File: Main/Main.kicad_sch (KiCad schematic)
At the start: 81 parts, among them J1 USB_B_Micro, J2 Micro_SD_Card, J3 Conn_01x03, J4 Conn_01x03, J5 Conn_01x03, J6 Conn_01x03, SW1 SW_Push, SW2 SW_Push, U1 RP2350A-QFN60, U10 LM75B, U11 MCS1802GS-50-Z, U12 MCS1802GS-50-Z, U13 MCS1802GS-50-Z, U14 LM2575-3.3BT, U2 W25Q128JVS, U3 AMS1117-3.3, U4 MMC5983MA, U5 ICM-42688-P, U6 INA226, U7 KX134-1211, U8 MS5611-01BA, U9 MCS1802GS-50-Z, Y1 ABM8-272-T3

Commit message: Added shunt footprint and small changes
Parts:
- removed R9: 2m, symbol Device:R_Shunt
- added R13: 2m, Resistor_SMD:R_1206_3216Metric, symbol Device:R
- C35, C36: footprint Capacitor_SMD:C_0805_2012Metric -> (none)
- D4: footprint Diode_SMD:D_0805_2012Metric -> (none)
- L2: footprint Inductor_SMD:L_0805_2012Metric -> (none)
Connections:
- net GND: now also U6.8 (Vbus), U6.9 (Vin-), R13.1
- net VSS: now also U6.10 (Vin+), R13.2
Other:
- note added: "High Precision 2mOhm Shunt"

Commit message: added button footprint
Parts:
- SW1, SW2: footprint (none) -> Button_Switch_SMD:SW_Push_SPST_NO_Alps_SKRK
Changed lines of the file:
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@@
 			)
 		)
-		(property "Footprint" ""
+		(property "Footprint" "Button_Switch_SMD:SW_Push_SPST_NO_Alps_SKRK"
 			(at 35.56 105.41 0)
 			(effects
@@
 			)
 		)
-		(property "Footprint" ""
+		(property "Footprint" "Button_Switch_SMD:SW_Push_SPST_NO_Alps_SKRK"
 			(at 139.7 115.57 0)
 			(effects

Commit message: updated usb footprint
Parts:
- J1: footprint (none) -> Connector_USB:USB_Micro-B_Amphenol_10118193-0001LF_Horizontal
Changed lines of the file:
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@@
 			)
 		)
-		(property "Footprint" ""
+		(property "Footprint" "Connector_USB:USB_Micro-B_Amphenol_10118193-0001LF_Horizontal"
 			(at 30.48 35.56 0)
 			(effects

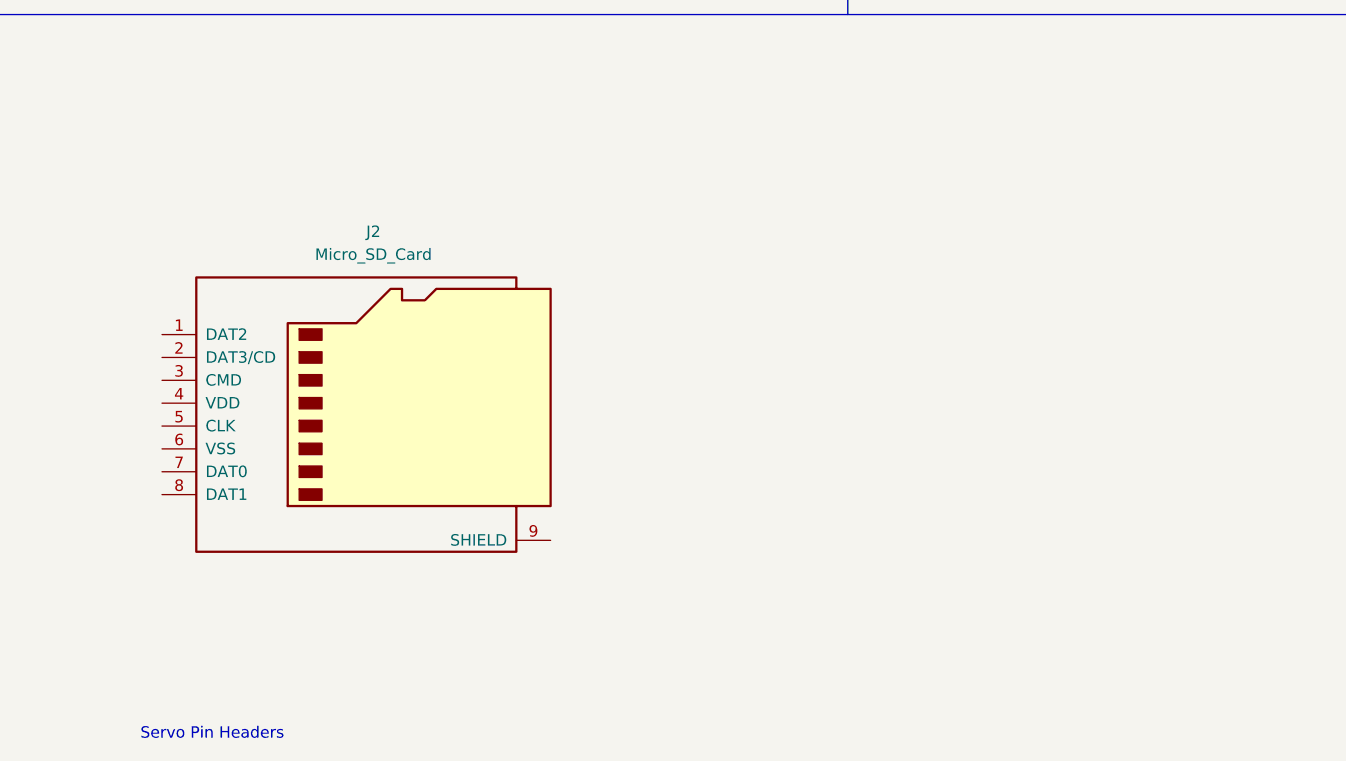
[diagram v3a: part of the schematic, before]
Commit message: SD and USB footprint and model updated
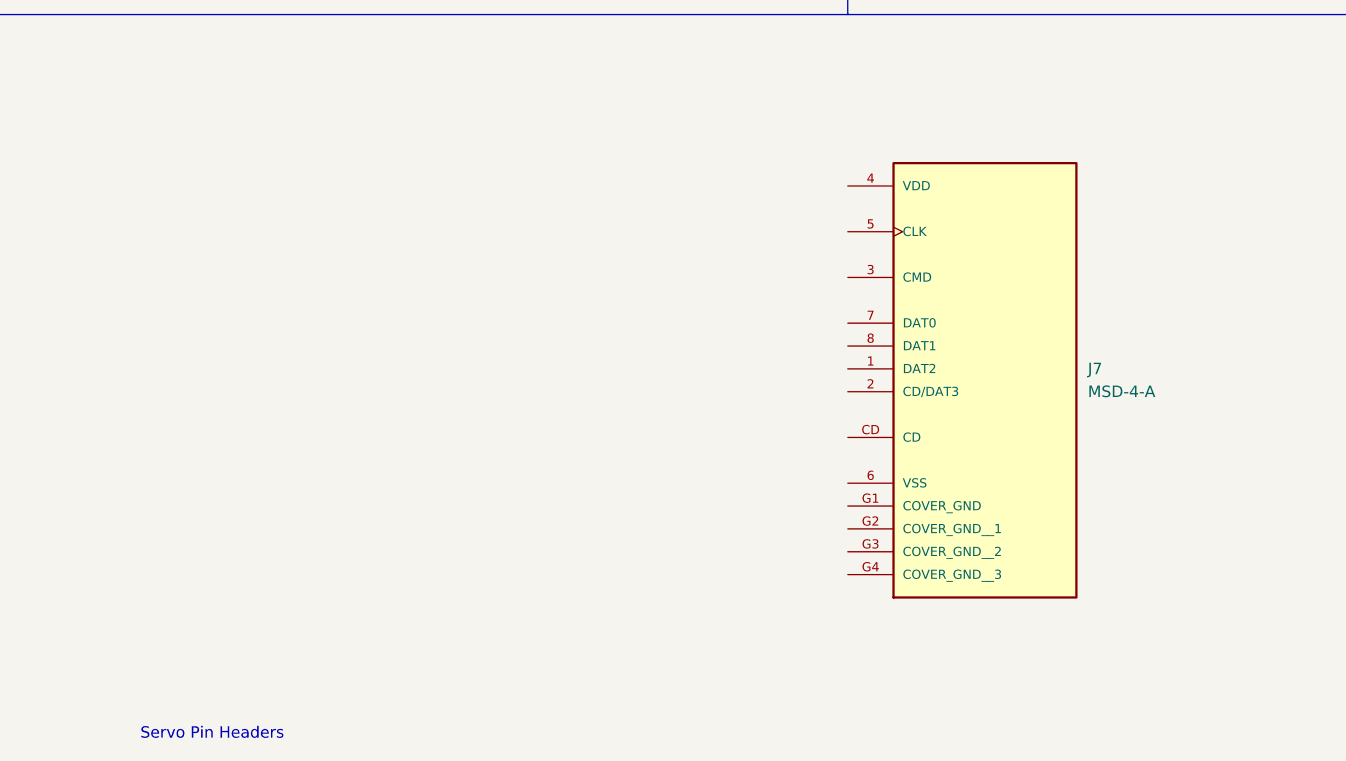
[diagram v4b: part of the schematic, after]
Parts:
- removed J2: Micro_SD_Card, symbol Connector:Micro_SD_Card
- added J7: MSD-4-A, otherComponents:CUI_MSD-4-A, symbol otherSymbols:MSD-4-A
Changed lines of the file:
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@@
 	)
 	(symbol
+		(lib_id "otherSymbols:MSD-4-A")
+		(at 391.16 267.97 0)
+		(unit 1)
+		(exclude_from_sim no)
+		(in_bom yes)
+		(on_board yes)
+		(dnp no)
+		(fields_autoplaced yes)
+		(property "Reference" "J7"
+			(at 402.59 270.5099 0)
+			(effects
+				(font
+					(size 1.27 1.27)
+				)
+				(justify left)
+			)
+		)
+		(property "Value" "MSD-4-A"
+			(at 402.59 273.0499 0)
+			(effects
+				(font
+					(size 1.27 1.27)
+				)
+				(justify left)
+			)
+		)
+		(property "Footprint" "otherComponents:CUI_MSD-4-A"
+			(at 391.16 267.97 0)
+			(effects
+				(font
+					(size 1.27 1.27)
+				)
+				(justify bottom)
+				(hide yes)
+			)
+		)
+		(property "Datasheet" ""
+			(at 391.16 267.97 0)
+			(effects
+				(font
+					(size 1.27 1.27)
+				)
+				(hide yes)
+			)
+		)
+		(property "Description" ""
+			(at 391.16 267.97 0)
+			(effects
+				(font
+					(size 1.27 1.27)
+				)
+				(hide yes)
+			)
+		)
+		(property "PARTREV" "1.0"
+			(at 391.16 267.97 0)
+			(effects
+				(font
+					(size 1.27 1.27)
+				)
+				(justify bottom)
+				(hide yes)
+			)
+		)
+		(property "STANDARD" "Manufacturer Recommendations"
+			(at 391.16 267.97 0)
+			(effects
+				(font
+					(size 1.27 1.27)
+				)
+				(justify bottom)
+				(hide yes)
+			)
+		)
+		(property "MAXIMUM_PACKAGE_HEIGHT" "2.00mm"
+			(at 391.16 267.97 0)
+			(effects
+				(font
+					(size 1.27 1.27)
+				)
+				(justify bottom)
+				(hide yes)
+			)
+		)
+		(property "MANUFACTURER" "CUI Devices"
+			(at 391.16 267.97 0)
+			(effects
+				(font
+					(size 1.27 1.27)
+				)
+				(justify bottom)
+				(hide yes)
+			)
+		)
+		(pin "3"
+		)
+		(pin "G1"
+		)
+		(pin "G4"
+		)
+		(pin "7"
+		)
+		(pin "8"
+		)
+		(pin "G3"
+		)
+		(pin "4"
+		)
+		(pin "1"
+		)
+		(pin "2"
+		)
+		(pin "CD"
+		)
+		(pin "G2"
+		)
+		(pin "5"
+		)
+		(pin "6"
+		)
+		(instances
+			(project ""
+				(path "/6b66026e-3aa1-4d5a-a331-be21386153c7"
+					(reference "J7")
+					(unit 1)
+				)
+			)
+		)
+	)
+	(symbol
 		(lib_id "power:GND")
 		(at 274.32 43.18 0)
@@
 					(unit 1)
 				)
-			)
-		)
-	)
-	(symbol
-		(lib_id "Connector:Micro_SD_Card")
-		(at 322.58 274.32 0)
-		(unit 1)
-		(exclude_from_sim no)
-		(in_bom yes)
-		(on_board yes)
-		(dnp no)
-		(fields_autoplaced yes)
-		(property "Reference" "J2"
-			(at 323.215 255.27 0)
-			(effects
-				(font
-					(size 1.27 1.27)
-				)
-			)
-		)
-		(property "Value" "Micro_SD_Card"
-			(at 323.215 257.81 0)
-			(effects
-				(font
-					(size 1.27 1.27)
-				)
-			)
-		)
-		(property "Footprint" ""
-			(at 351.79 266.7 0)
-			(effects
-				(font
-					(size 1.27 1.27)
-				)
-				(hide yes)
-			)
-		)
-		(property "Datasheet" "https://www.we-online.com/components/products/datasheet/693072010801.pdf"
-			(at 322.58 274.32 0)
-			(effects
-				(font
-					(size 1.27 1.27)
-				)
-				(hide yes)
-			)
-		)
-		(property "Description" "Micro SD Card Socket"
-			(at 322.58 274.32 0)
-			(effects
-				(font
-					(size 1.27 1.27)
-				)
-				(hide yes)
-			)
-		)
-		(pin "9"
-		)
-		(pin "2"
-		)
-		(pin "3"
-		)
-		(pin "4"
-		)
-		(pin "5"
-		)
-		(pin "1"
-		)
-		(pin "6"
-		)
-		(pin "8"
-		)
-		(pin "7"
-		)
-		(instances
-			(project ""
-				(path "/6b66026e-3aa1-4d5a-a331-be21386153c7"
-					(reference "J2")
-					(unit 1)
-				)

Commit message: added xt60 connector
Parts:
- added J2: Conn_01x02, Connector_AMASS:AMASS_XT60-M_1x02_P7.20mm_Vertical, symbol Connector_Generic:Conn_01x02
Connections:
- net GND: now also J2.1 (Pin_1)
- net VIN: now also U11.1 (IP+), U11.2 (IP+), U12.1 (IP+), U12.2 (IP+), U13.1 (IP+), U13.2 (IP+), U9.1 (IP+), U9.2 (IP+), J2.2 (Pin_2)
- net current +: no longer U11.1 (IP+), U11.2 (IP+), U13.1 (IP+), U13.2 (IP+)
- net current -2: no longer U9.1 (IP+), U9.2 (IP+)
- net current -3: no longer U12.1 (IP+), U12.2 (IP+)
- net VOUT: no longer names the net of C36.1, L2.2, U14.4 (FB)
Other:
- note added: "figure out connection of 3.3v sources"

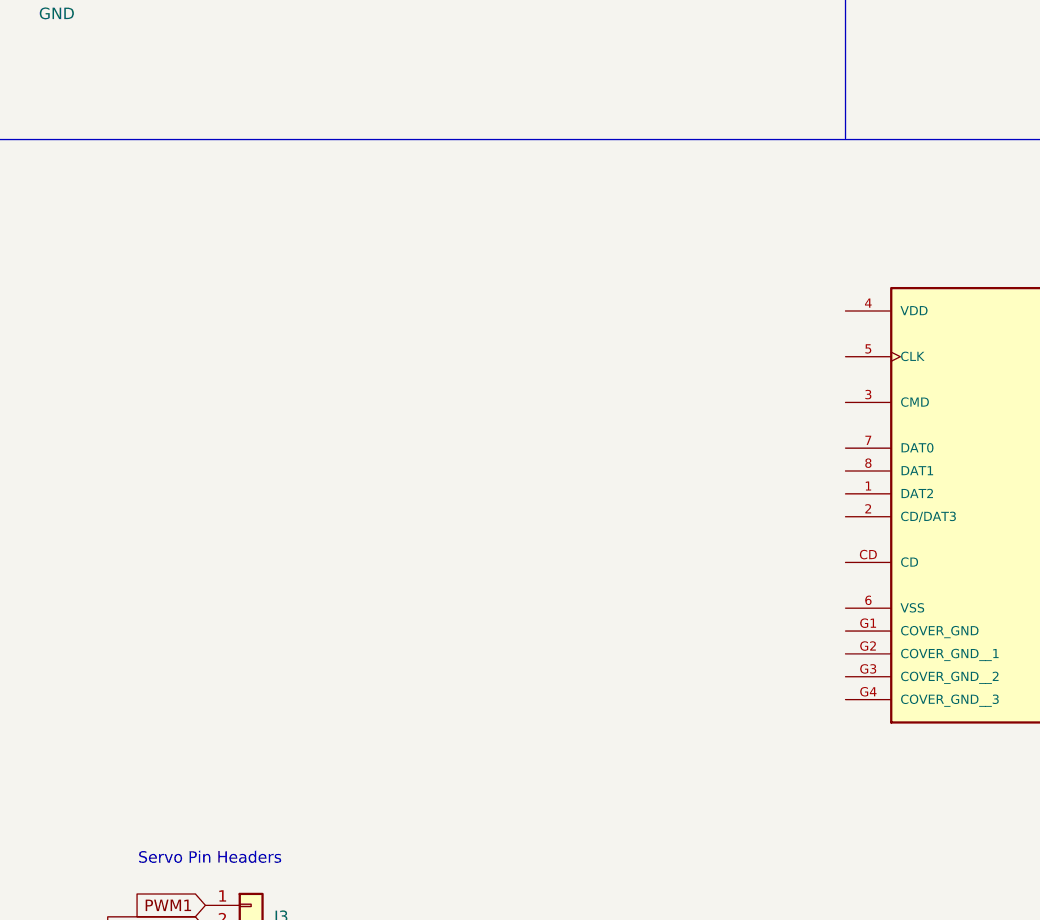
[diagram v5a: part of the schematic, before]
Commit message: added schematic sd card
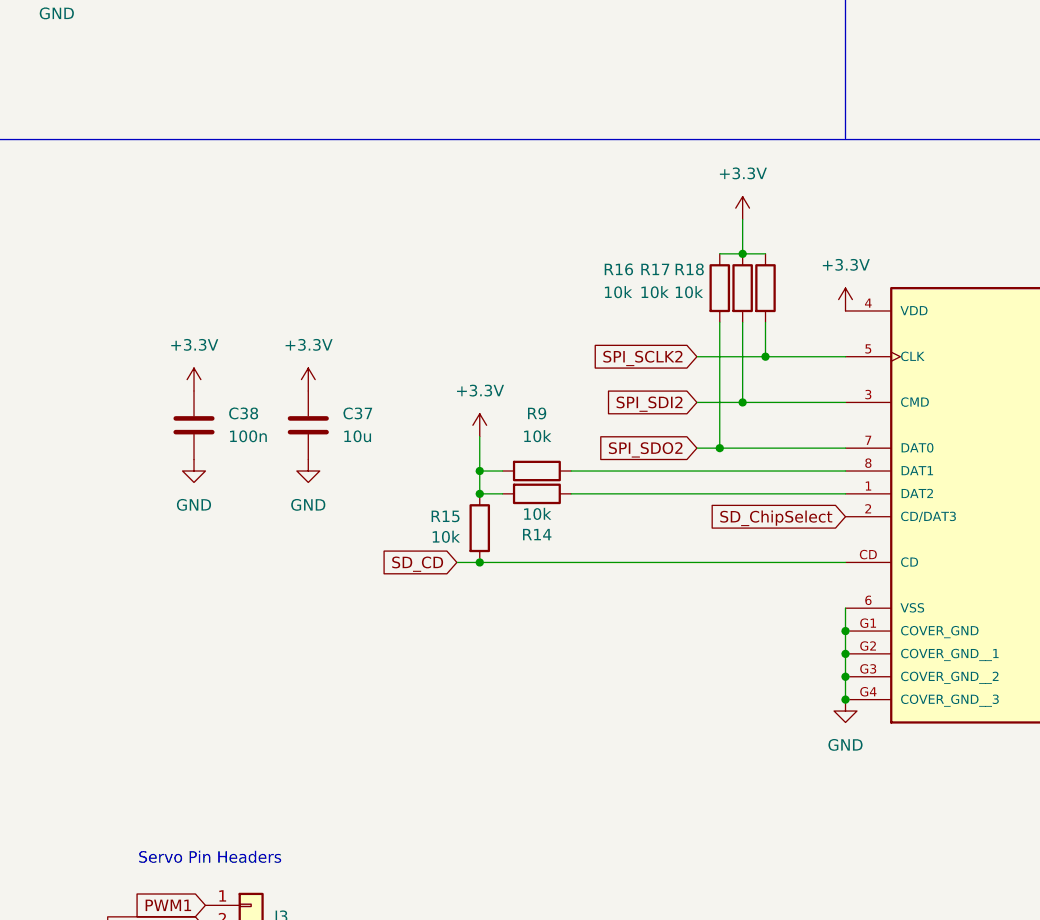
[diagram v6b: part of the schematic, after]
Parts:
- added C37: 10u, symbol Device:C
- added C38: 100n, symbol Device:C
- added R14, R15, R16, R17, R18, R9: 10k, symbol Device:R
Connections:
- net +3.3V: now also J7.4 (VDD), C37.1, C38.1, R14.2, R15.1, R16.1, R17.1, R18.1, R9.2
- net GND: now also J7.6 (VSS), J7.G1 (COVER_GND), J7.G2 (COVER_GND__1), J7.G3 (COVER_GND__2), J7.G4 (COVER_GND__3), C37.2, C38.2
- net at J7.1 (DAT2): now also R14.1
- net SD_ChipSelect: now reaches J7.2 (CD/DAT3)
- net SPI_SDI2: now reaches J7.3 (CMD)
- net SPI_SDI2: now also R17.2
- net SPI_SCLK2: now reaches J7.5 (CLK)
- net SPI_SCLK2: now also R18.2
- net SPI_SDO2: now reaches J7.7 (DAT0)
- net SPI_SDO2: now also R16.2
- net at J7.8 (DAT1): now also R9.1
- net SD_CD: now reaches J7.CD
- net SD_CD: now also R15.2

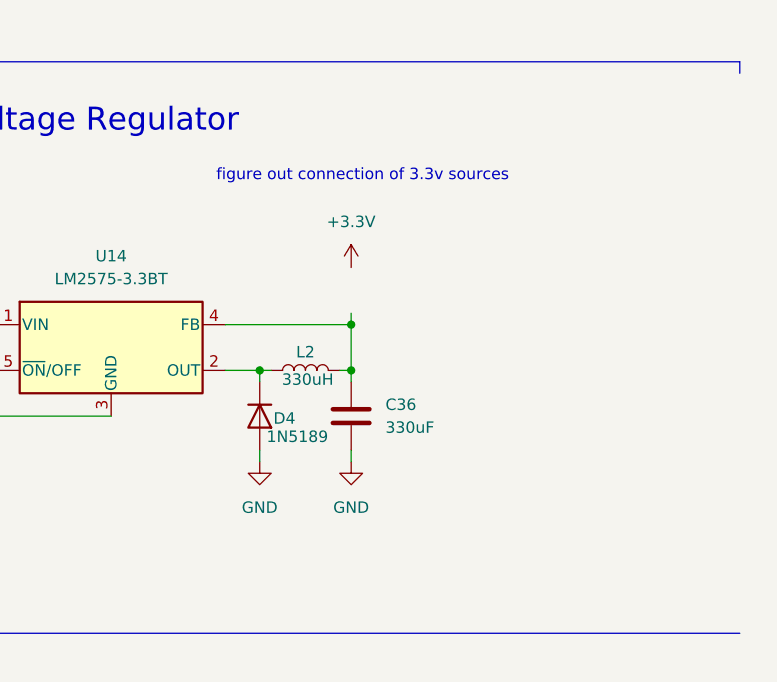
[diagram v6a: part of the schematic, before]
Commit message: added p-channel mosfet for power control
USB plugged in -> VBUS high, Vgs on mosfet = 0 -> mosfet off, disconect linear regulator from 3.3v system rails
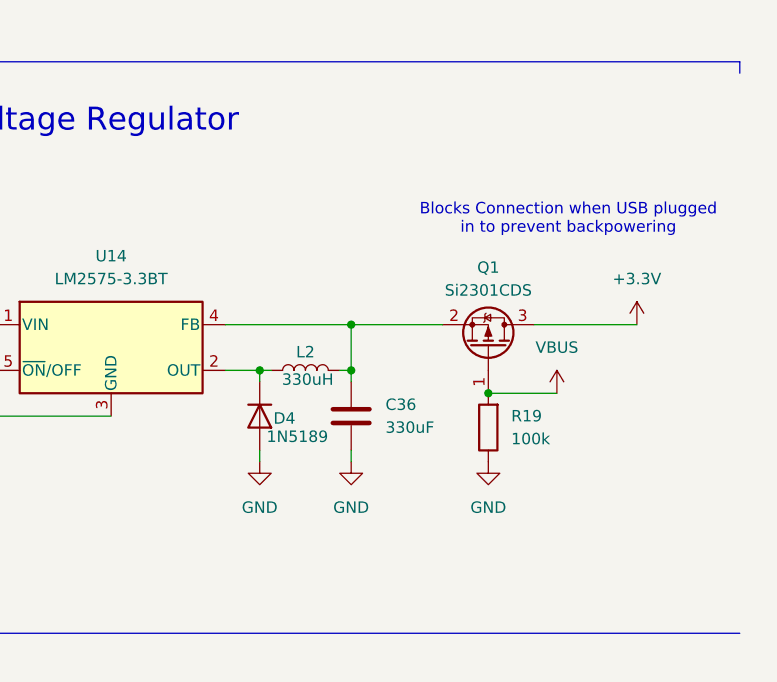
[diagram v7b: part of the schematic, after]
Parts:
- added Q1: Si2301CDS, Package_TO_SOT_SMD:SOT-23, symbol Transistor_FET:Si2319CDS
- added R19: 100k, Resistor_SMD:R_0402_1005Metric, symbol Device:R
- C37: footprint (none) -> Capacitor_SMD:C_0805_2012Metric
- C38: footprint (none) -> Capacitor_SMD:C_0402_1005Metric
- R14, R15, R16, R17, R18, R9: footprint (none) -> Resistor_SMD:R_0402_1005Metric
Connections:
- net +3.3V: now also Q1.3 (D)
- net GND: now also R19.1
- net VBUS: now also Q1.1 (G), R19.2
- net at C36.1, L2.2, U14.4 (FB): now also Q1.2 (S)
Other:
- note added: "Blocks Connection when USB plugged in to prevent backpowering"
- note removed: "figure out connection of 3.3v sources"

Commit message: changed voltage regulator
new voltage regulator chip(smaller + more effecient) and supporting components
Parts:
- removed C35: 100uF, symbol Device:C
- removed C36: 330uF, symbol Device:C
- removed D4: 1N5189, symbol Device:D
- removed L2: 330uH, symbol Device:L
- removed Q1: Si2301CDS, Package_TO_SOT_SMD:SOT-23, symbol Transistor_FET:Si2319CDS
- removed R19: 100k, Resistor_SMD:R_0402_1005Metric, symbol Device:R
- removed U14: LM2575-3.3BT, Package_TO_SOT_SMD:TO-263-5_TabPin3, symbol Regulator_Switching:LM2575-3.3BT
- added C39: 10u, Capacitor_SMD:C_0805_2012Metric, symbol Device:C
- added C40: 100n, Capacitor_SMD:C_0402_1005Metric, symbol Device:C
- added C41: 22u, Capacitor_SMD:C_0805_2012Metric, symbol Device:C
- added L3: 3.3u, Inductor_SMD:L_1008_2520Metric_Pad1.43x2.20mm_HandSolder, symbol Device:L
- added Q2: Si2301CDS, Package_TO_SOT_SMD:SOT-23, symbol Transistor_FET:Si2319CDS
- added R20: 30k, Resistor_SMD:R_0603_1608Metric, symbol Device:R
- added R21: 10k, Resistor_SMD:R_0402_1005Metric, symbol Device:R
- added R22: 100k, Resistor_SMD:R_0402_1005Metric, symbol Device:R
- added R23: 1k, Resistor_SMD:R_0402_1005Metric, symbol Device:R
- added U15: AP62150WU, Package_TO_SOT_SMD:TSOT-23-6, symbol Regulator_Switching:AP62150WU
- J2: value Conn_01x02 -> XT60
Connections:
- net current + is gone; now on net VIN: U12.3 (IP-), U12.4 (IP-), U9.3 (IP-), U9.4 (IP-)
- net +3.3V: now also Q2.3 (D)
- net GND: now also C39.2, C41.2, R21.2, R22.1, U15.1 (GND)
- net VBUS: now also Q2.1 (G), R22.2
- net VIN: now also C39.1, U15.3 (VIN); no longer U12.1 (IP+), U12.2 (IP+), U9.1 (IP+), U9.2 (IP+)
- net current -2: now also U9.1 (IP+), U9.2 (IP+)
- net current -3: now also U12.1 (IP+), U12.2 (IP+)
- new net: C41.1, L3.1, Q2.2 (S), R20.1
- new net: C40.1, L3.2, U15.2 (SW)
- new net: C40.2, U15.6 (BST)
- new net: R20.2, R23.1
- new net: R21.1, R23.2, U15.4 (FB)
- no-connect marks 9 -> 10
